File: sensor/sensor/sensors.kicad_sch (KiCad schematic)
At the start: 23 parts, among them IC1 VL53L4CDV0DH_1, IC2 ISL29125IROZ-T7, J4 Conn_01x03_Socket, J5 Conn_01x03_Socket, J6 Conn_01x03_Socket, J7 Conn_01x03_Socket, U4 PCA9536DP, U6 ICM-20602

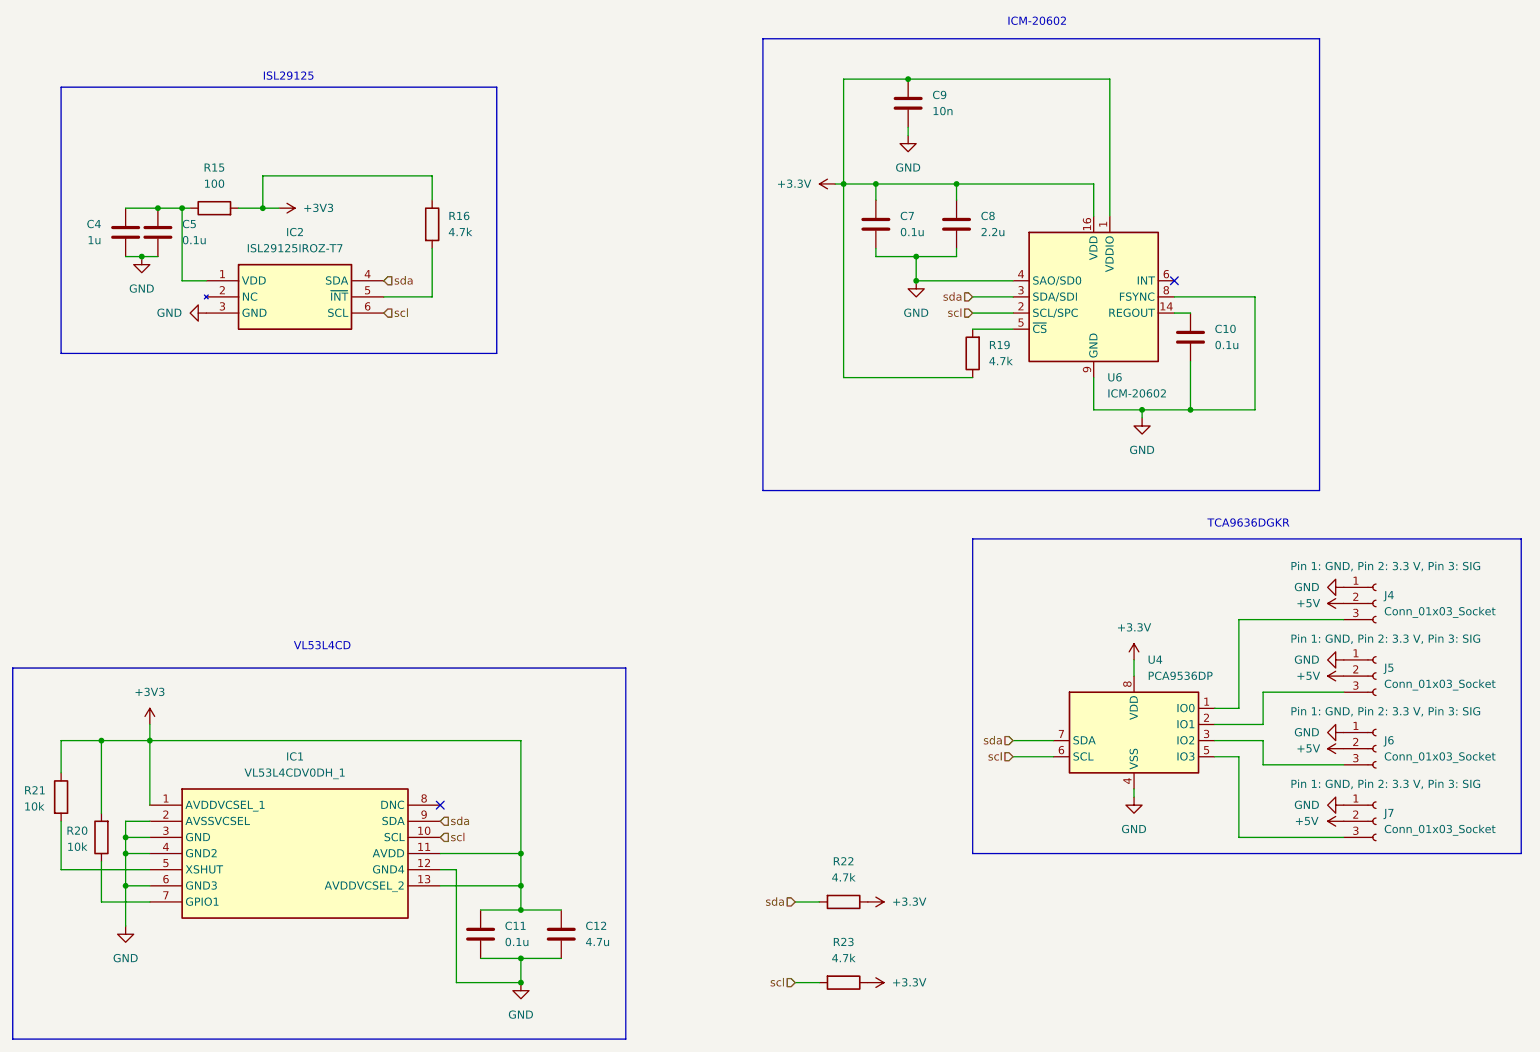
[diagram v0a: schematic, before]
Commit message: sensor pcb layout, deleted gpio ic
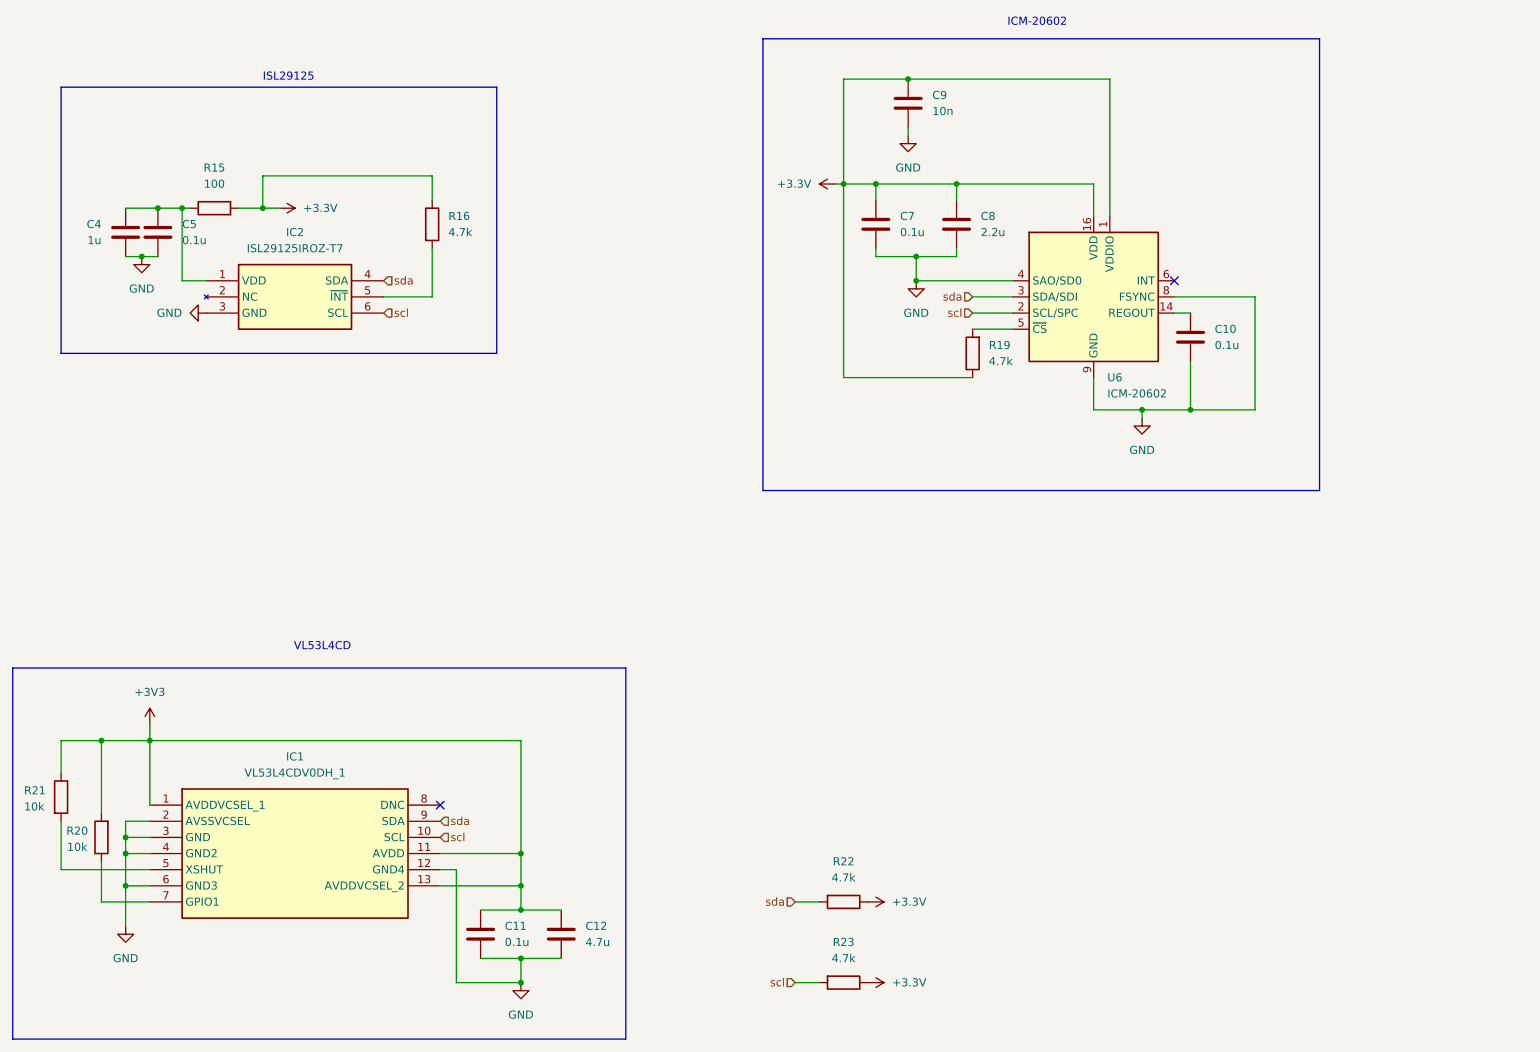
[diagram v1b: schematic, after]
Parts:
- removed J4, J5, J6, J7: Conn_01x03_Socket, Connector_PinSocket_2.54mm:PinSocket_1x03_P2.54mm_Vertical, symbol Connector:Conn_01x03_Socket
- removed U4: PCA9536DP, Package_SO:TSSOP-8_3x3mm_P0.65mm, symbol Interface_Expansion:PCA9536DP
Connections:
- net +3.3V: now also R15.2, R16.1
- net +3V3: no longer R15.2, R16.1
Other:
- note removed: "TCA9636DGKR"

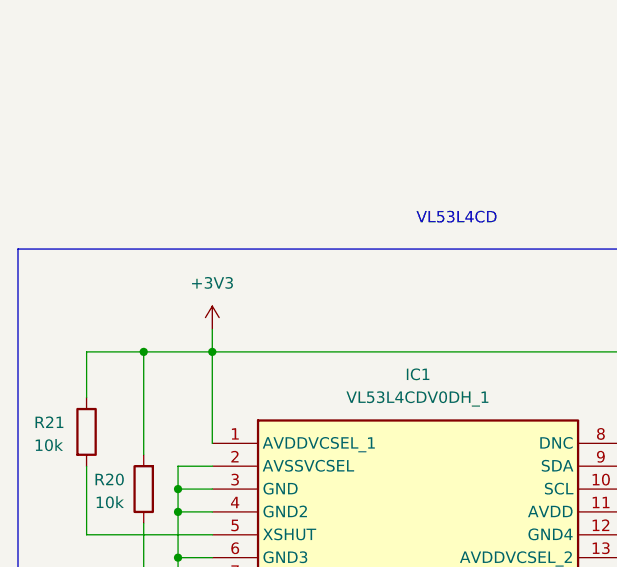
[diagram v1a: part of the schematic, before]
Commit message: sensor pcb layout
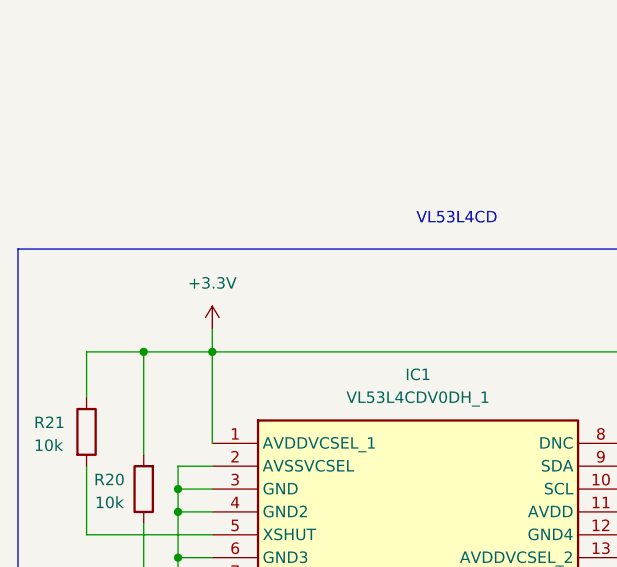
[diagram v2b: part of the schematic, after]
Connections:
- net +3V3 is gone; now on net +3.3V: C11.1, C12.1, IC1.1 (AVDDVCSEL_1), IC1.11 (AVDD), IC1.13 (AVDDVCSEL_2), R20.2, R21.1
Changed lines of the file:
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@@
 			)
 		)
-		(property "Value" "+3V3"
+		(property "Value" "+3.3V"
 			(at 48.26 132.08 0)
 			(effects
